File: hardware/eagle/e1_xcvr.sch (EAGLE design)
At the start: 36 parts

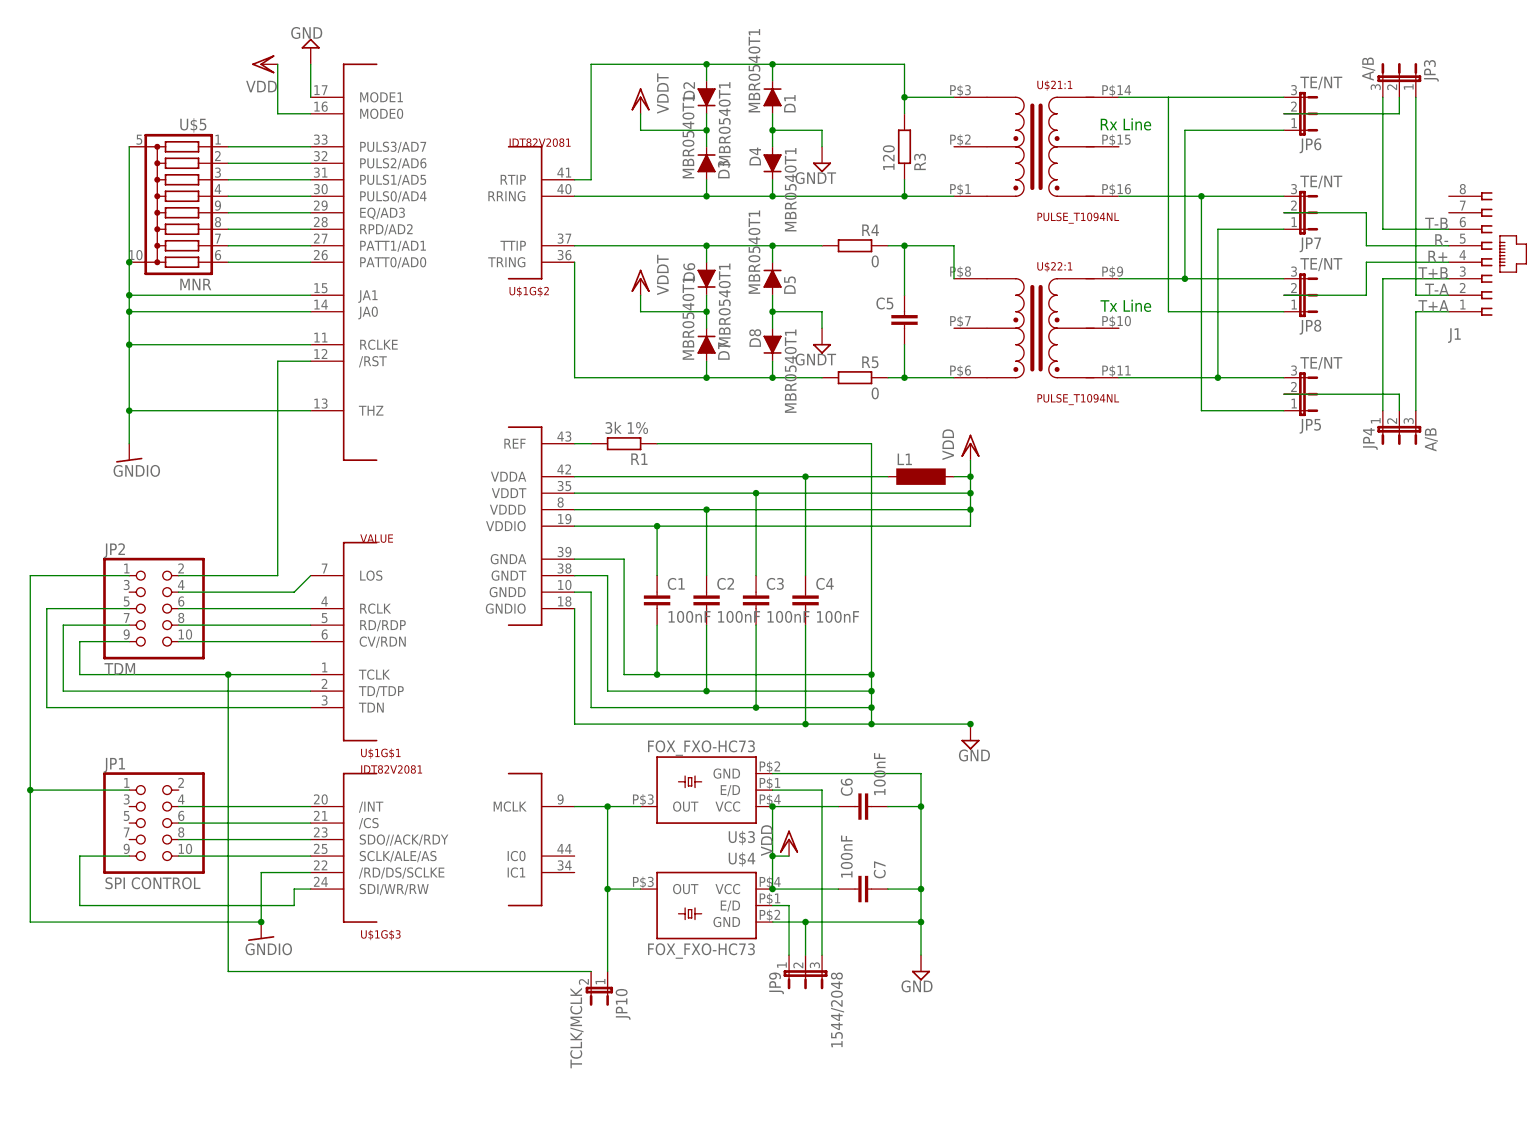
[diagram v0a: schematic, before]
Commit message: Add LDO, remove jumpers, 3nd RJ45, ...
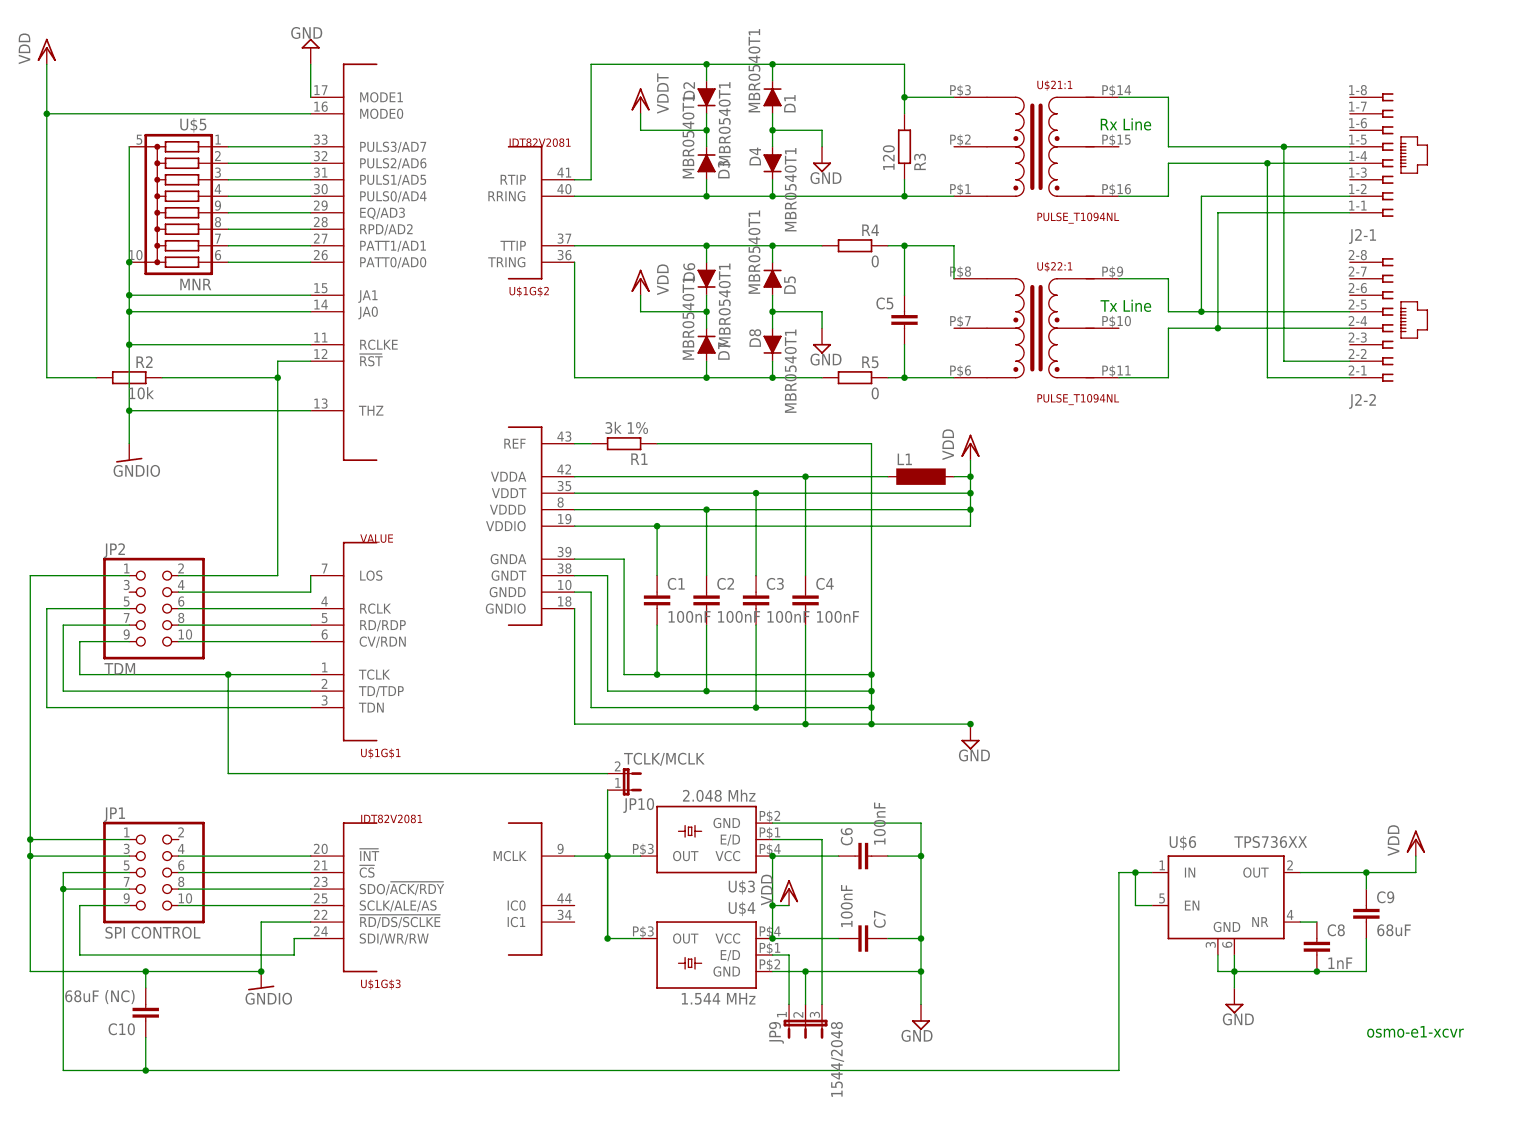
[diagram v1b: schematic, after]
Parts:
- removed J1: (no value), con-amp:520251-4
- removed JP3, JP4: A/B, jumper:JP2E
- removed JP5, JP6, JP7, JP8: TE/NT, jumper:JP2E
- added C10: 68uF (NC), rcl:C-EUC1206K
- added C8: 1nF, rcl:C-EUC0603
- added C9: 68uF, rcl:C-EUC1206K
- added J2: (no value), con-amp:557560-1
- added R2: 10k, rcl:R-EU_R0603
- added U$6: TPS736XX, laforge:TPS736XX
- U$3: value FOX_FXO-HC73 -> 2.048 Mhz
- U$4: value FOX_FXO-HC73 -> 1.544 MHz
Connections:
- removed net GNDT: D1.A, D4.A
- removed net N$24: C6.1, C7.2, U$3.VCC, U$4.VCC
- removed net N$33: JP5.3, JP7.1, U$22:1.P$4
- removed net N$42: JP6.1, JP8.3, U$22:1.P$6
- removed net R+: J1.4, JP8.2
- removed net R-: J1.5, JP7.2
- removed net T+A: J1.1, JP4.3
- removed net T+B: J1.3, JP4.1
- removed net T-A: J1.2, JP3.1
- removed net T-B: J1.6, JP3.3
- new net N$34: J2-1.4, J2-2.1, U$21:1.P$4
- new net VIN: C10.1, JP1.5, JP1.7, U$6.EN, U$6.IN
- net GND: now also C10.2, C8.2, C9.2, D1.A, D4.A, JP1.1, JP1.3, JP2.1, U$1G$3.!RD/DS/SCLKE, U$6.GND, U$6.GND1
- net GNDIO: no longer JP1.1, JP2.1, U$1G$3./RD/DS/SCLKE
- net N$17: now also R2.1, U$1G$4.!RST; no longer U$1G$4./RST
- net N$19: now also U$1G$3.!INT; no longer U$1G$3./INT
- net N$20: now also U$1G$3.!CS; no longer U$1G$3./CS
- net N$21: now also U$1G$3.SDO/!ACK/RDY; no longer U$1G$3.SDO//ACK/RDY
- net N$32: now also J2-1.2, J2-2.5, U$22:1.P$6; no longer JP5.1, JP7.3, U$21:1.P$4
- net N$36: now also J2-1.1, J2-2.4, U$22:1.P$4; no longer JP4.2, JP5.2
- net N$37: now also C8.1, U$6.NR; no longer JP3.2, JP6.2
- net N$40: now also J2-1.5, J2-2.2; no longer JP6.3, JP8.1
- net VDD: now also C6.1, C7.2, C9.1, R2.2, U$3.VCC, U$4.VCC, U$6.OUT
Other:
- note added: "osmo-e1-xcvr"
- moved on the sheet: C6, C7, JP1, JP10, JP9, U$1G$3, U$3, U$4

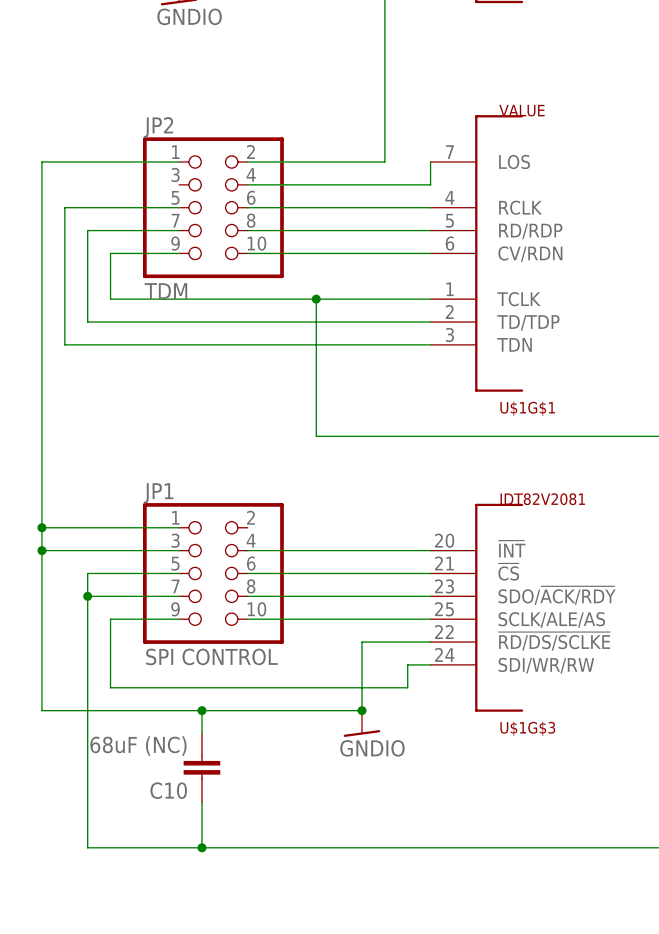
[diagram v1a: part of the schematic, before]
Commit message: re-wire SPI connector to reflect pin-out of Olimex devel board UEXT
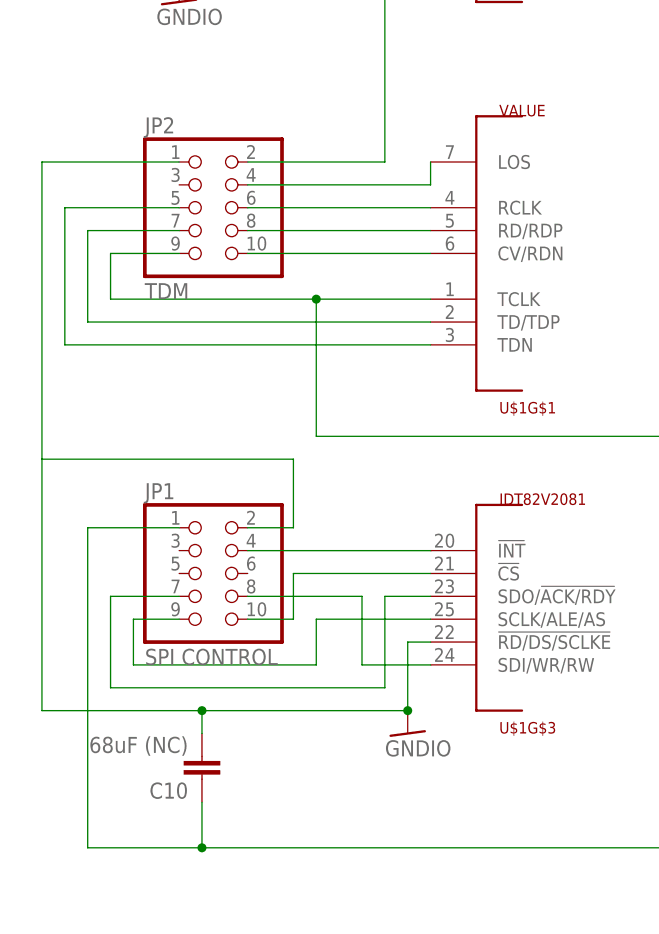
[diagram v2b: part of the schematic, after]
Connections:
- removed net N$26: JP1.10, U$1G$3.SCLK/ALE/AS
- new net N$19: JP1.8, U$1G$3.SDI/WR/RW
- net GND: now also JP1.2; no longer JP1.1, JP1.3
- net N$20: now also JP1.10; no longer JP1.6
- net N$21: now also JP1.7; no longer JP1.8
- net N$22: now also U$1G$3.SCLK/ALE/AS; no longer U$1G$3.SDI/WR/RW
- net VIN: now also JP1.1; no longer JP1.5, JP1.7

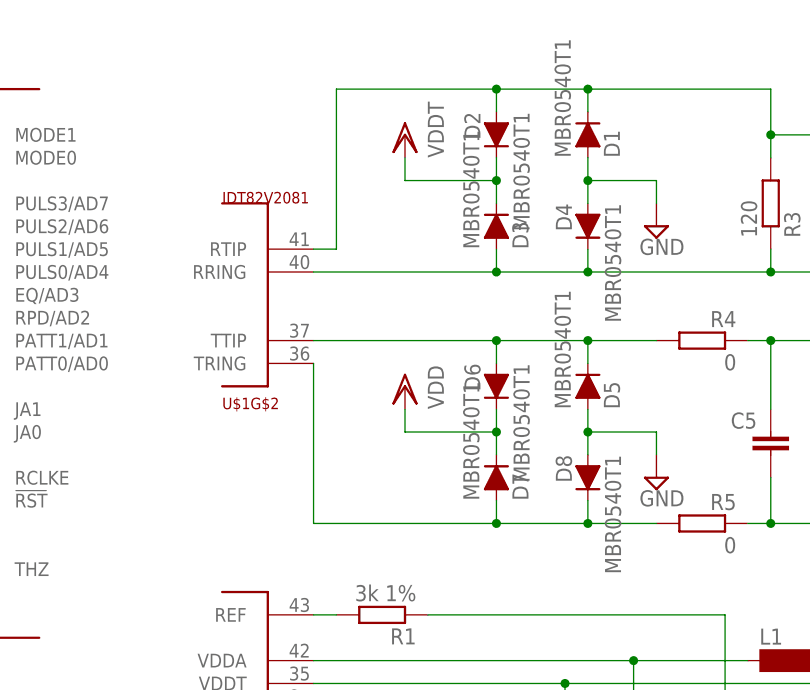
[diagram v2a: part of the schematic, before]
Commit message: add 4 test pads for RTIP/RRING/TTIP/TRING
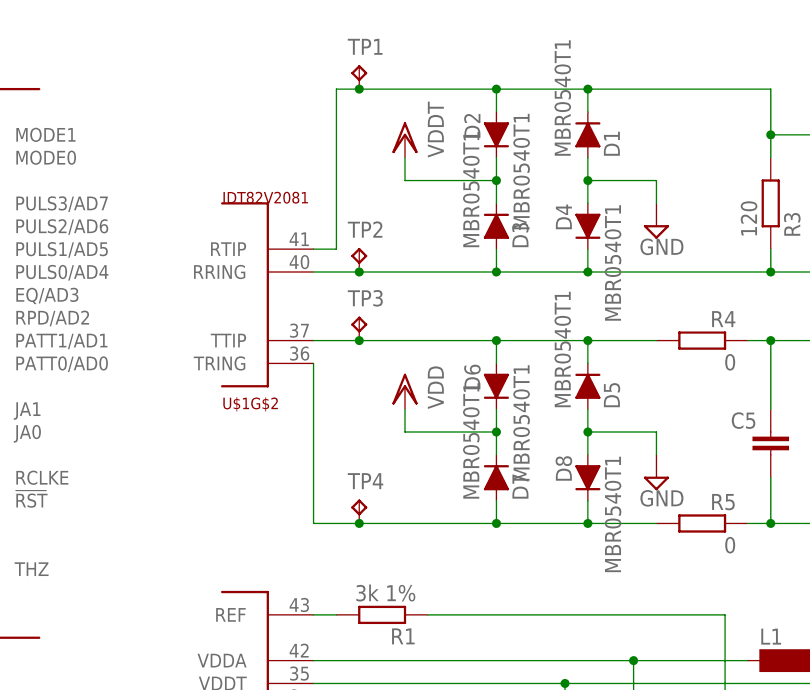
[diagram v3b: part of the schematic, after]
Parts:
- added TP1, TP2, TP3, TP4: TPPAD1-13, testpad:TPPAD1-13
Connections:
- net N$25: now also TP3.TP
- net N$27: now also TP1.TP
- net N$28: now also TP2.TP
- net N$30: now also TP4.TP
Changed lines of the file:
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@@
 <part name="VDD1" library="supply1" deviceset="VDD" device=""/>
 <part name="C10" library="rcl" deviceset="C-EU" device="C1206K" value="68uF (NC)"/>
+<part name="TP1" library="testpad" deviceset="TP" device="PAD1-13"/>
+<part name="TP2" library="testpad" deviceset="TP" device="PAD1-13"/>
+<part name="TP3" library="testpad" deviceset="TP" device="PAD1-13"/>
+<part name="TP4" library="testpad" deviceset="TP" device="PAD1-13"/>
 </parts>
 <sheets>
@@
 <instance part="VDD1" gate="G$1" x="208.28" y="86.36"/>
 <instance part="C10" gate="G$1" x="12.7" y="58.42" rot="R180"/>
+<instance part="TP1" gate="G$1" x="83.82" y="208.28"/>
+<instance part="TP2" gate="G$1" x="83.82" y="187.96"/>
+<instance part="TP3" gate="G$1" x="83.82" y="180.34"/>
+<instance part="TP4" gate="G$1" x="83.82" y="160.02"/>
 </instances>
 <busses>
@@
 <junction x="99.06" y="205.74"/>
 <junction x="109.22" y="205.74"/>
-<wire x1="99.06" y1="205.74" x2="81.28" y2="205.74" width="0.1524" layer="91"/>
+<wire x1="99.06" y1="205.74" x2="83.82" y2="205.74" width="0.1524" layer="91"/>
+<wire x1="83.82" y1="205.74" x2="81.28" y2="205.74" width="0.1524" layer="91"/>
 <wire x1="81.28" y1="205.74" x2="81.28" y2="187.96" width="0.1524" layer="91"/>
 <pinref part="U$1" gate="G$2" pin="RTIP"/>
 <wire x1="81.28" y1="187.96" x2="78.74" y2="187.96" width="0.1524" layer="91"/>
+<pinref part="TP1" gate="G$1" pin="TP"/>
+<junction x="83.82" y="205.74"/>
 </segment>
 </net>
@@
 <junction x="109.22" y="185.42"/>
 <pinref part="U$1" gate="G$2" pin="RRING"/>
-<wire x1="99.06" y1="185.42" x2="78.74" y2="185.42" width="0.1524" layer="91"/>
+<wire x1="99.06" y1="185.42" x2="83.82" y2="185.42" width="0.1524" layer="91"/>
+<pinref part="TP2" gate="G$1" pin="TP"/>
+<wire x1="83.82" y1="185.42" x2="78.74" y2="185.42" width="0.1524" layer="91"/>
+<junction x="83.82" y="185.42"/>
 </segment>
 </net>
@@
 <wire x1="99.06" y1="177.8" x2="99.06" y2="175.26" width="0.1524" layer="91"/>
 <junction x="99.06" y="177.8"/>
-<wire x1="99.06" y1="177.8" x2="78.74" y2="177.8" width="0.1524" layer="91"/>
+<wire x1="99.06" y1="177.8" x2="83.82" y2="177.8" width="0.1524" layer="91"/>
 <pinref part="U$1" gate="G$2" pin="TTIP"/>
 <pinref part="R4" gate="G$1" pin="2"/>
+<wire x1="83.82" y1="177.8" x2="78.74" y2="177.8" width="0.1524" layer="91"/>
 <wire x1="116.84" y1="177.8" x2="109.22" y2="177.8" width="0.1524" layer="91"/>
 <junction x="109.22" y="177.8"/>
+<pinref part="TP3" gate="G$1" pin="TP"/>
+<junction x="83.82" y="177.8"/>
 </segment>
 </net>
@@
 <wire x1="99.06" y1="157.48" x2="99.06" y2="160.02" width="0.1524" layer="91"/>
 <junction x="99.06" y="157.48"/>
-<wire x1="99.06" y1="157.48" x2="78.74" y2="157.48" width="0.1524" layer="91"/>
+<wire x1="99.06" y1="157.48" x2="83.82" y2="157.48" width="0.1524" layer="91"/>
 <pinref part="U$1" gate="G$2" pin="TRING"/>
+<wire x1="83.82" y1="157.48" x2="78.74" y2="157.48" width="0.1524" layer="91"/>
 <wire x1="78.74" y1="157.48" x2="78.74" y2="175.26" width="0.1524" layer="91"/>
 <pinref part="R5" gate="G$1" pin="2"/>
 <wire x1="116.84" y1="157.48" x2="109.22" y2="157.48" width="0.1524" layer="91"/>
 <junction x="109.22" y="157.48"/>
-</segment>
-</net>
+<pinref part="TP4" gate="G$1" pin="TP"/>
+<junction x="83.82" y="157.48"/>
+</segment>
+</net>

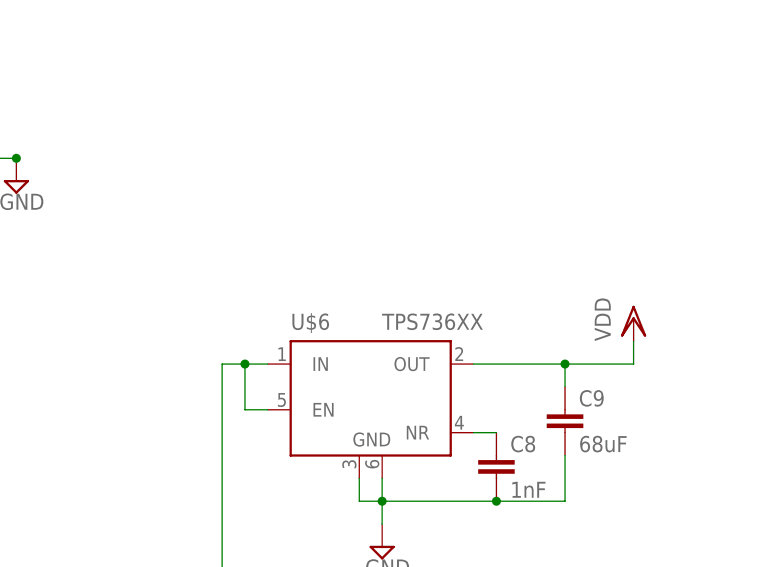
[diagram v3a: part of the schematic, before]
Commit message: add solder jumper to bypass TPS736XX (if it is not populated)
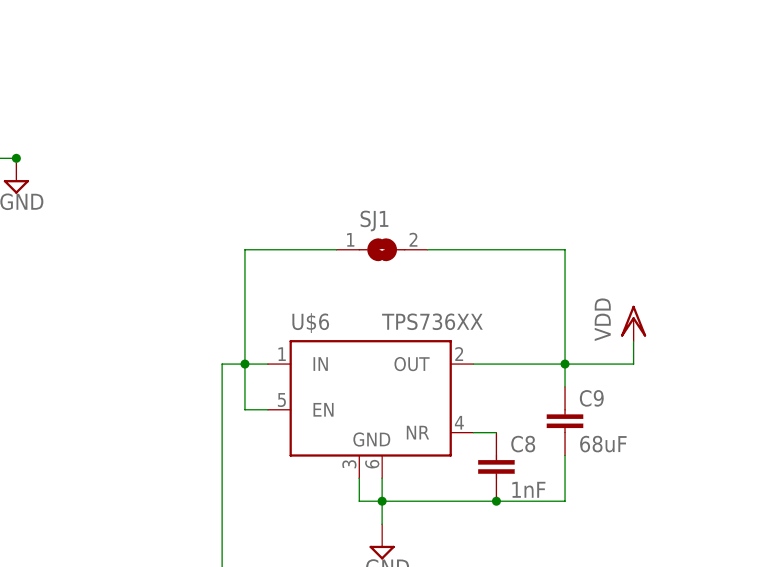
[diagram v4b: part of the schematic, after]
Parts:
- added SJ1: (no value), jumper:SJ
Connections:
- net VDD: now also SJ1.2
- net VIN: now also SJ1.1
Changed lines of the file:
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@@
 <part name="TP3" library="testpad" deviceset="TP" device="PAD1-13"/>
 <part name="TP4" library="testpad" deviceset="TP" device="PAD1-13"/>
+<part name="SJ1" library="jumper" deviceset="SJ" device=""/>
 </parts>
 <sheets>
@@
 <instance part="TP3" gate="G$1" x="83.82" y="180.34"/>
 <instance part="TP4" gate="G$1" x="83.82" y="160.02"/>
+<instance part="SJ1" gate="1" x="180.34" y="93.98"/>
 </instances>
 <busses>
@@
 <pinref part="VDD1" gate="G$1" pin="VDD"/>
 <wire x1="208.28" y1="81.28" x2="208.28" y2="83.82" width="0.1524" layer="91"/>
+<pinref part="SJ1" gate="1" pin="2"/>
+<wire x1="185.42" y1="93.98" x2="200.66" y2="93.98" width="0.1524" layer="91"/>
+<wire x1="200.66" y1="93.98" x2="200.66" y2="81.28" width="0.1524" layer="91"/>
 </segment>
 </net>
@@
 <pinref part="JP1" gate="A" pin="1"/>
 <wire x1="0" y1="86.36" x2="10.16" y2="86.36" width="0.1524" layer="91"/>
-</segment>
-</net>
+<wire x1="165.1" y1="81.28" x2="165.1" y2="93.98" width="0.1524" layer="91"/>
+<pinref part="SJ1" gate="1" pin="1"/>
+<wire x1="165.1" y1="93.98" x2="175.26" y2="93.98" width="0.1524" layer="91"/>
+</segment>
+</net>

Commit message: just name some signals/networks
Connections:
- net N$18 renamed MCLK
- net N$25 renamed TTIP
- net N$27 renamed RTIP
- net N$28 renamed RRING
- net N$30 renamed TRING
- net N$7 renamed TCLK
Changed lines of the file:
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@@
 </segment>
 </net>
-<net name="VDD" class="0">
+<net name="VDD" class="1">
 <segment>
 <pinref part="U$1" gate="G$4" pin="MODE0"/>
@@
 </segment>
 </net>
-<net name="N$7" class="0">
+<net name="TCLK" class="0">
 <segment>
 <pinref part="U$1" gate="G$1" pin="TCLK"/>
@@
 </segment>
 </net>
-<net name="N$27" class="0">
+<net name="RTIP" class="0">
 <segment>
 <pinref part="U$2" gate="1:1" pin="P$3"/>
@@
 </segment>
 </net>
-<net name="N$28" class="0">
+<net name="RRING" class="0">
 <segment>
 <pinref part="U$2" gate="1:1" pin="P$1"/>
@@
 </segment>
 </net>
-<net name="N$25" class="0">
+<net name="TTIP" class="0">
 <segment>
 <pinref part="D5" gate="G$1" pin="C"/>
@@
 </segment>
 </net>
-<net name="N$30" class="0">
+<net name="TRING" class="0">
 <segment>
 <pinref part="D8" gate="G$1" pin="C"/>
@@
 </segment>
 </net>
-<net name="N$18" class="0">
+<net name="MCLK" class="0">
 <segment>
 <pinref part="U$4" gate="G$1" pin="OUT"/>
